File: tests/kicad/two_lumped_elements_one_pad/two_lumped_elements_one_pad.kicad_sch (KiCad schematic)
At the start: 1 part

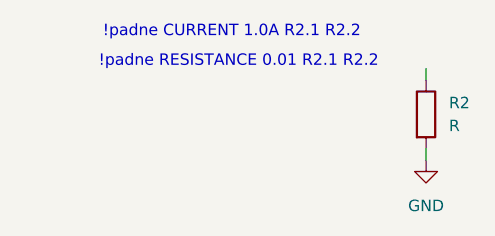
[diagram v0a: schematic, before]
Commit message: feat: Richer directive syntax
This commit adds support for named directive parameters. No more
guessing which parameter is the positive terminal positive and which is the
negative terminal!
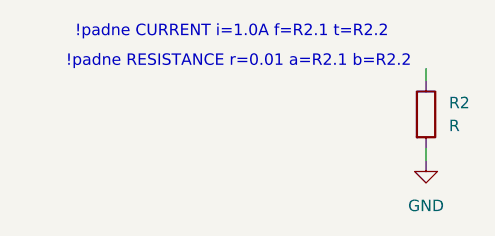
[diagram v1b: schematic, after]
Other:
- note added: "!padne CURRENT i=1.0A f=R2.1 t=R2.2"
- note added: "!padne RESISTANCE r=0.01 a=R2.1 b=R2.2"
- note removed: "!padne CURRENT 1.0A R2.1 R2.2"
- note removed: "!padne RESISTANCE 0.01 R2.1 R2.2"
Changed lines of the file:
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@@
 		)
 	)
-	(text "!padne CURRENT 1.0A R2.1 R2.2"
+	(text "!padne CURRENT i=1.0A f=R2.1 t=R2.2"
 		(exclude_from_sim no)
 		(at 118.11 96.266 0)
@@
 		)
 	)
-	(text "!padne RESISTANCE 0.01 R2.1 R2.2"
+	(text "!padne RESISTANCE r=0.01 a=R2.1 b=R2.2"
 		(exclude_from_sim no)
 		(at 118.872 99.568 0)
